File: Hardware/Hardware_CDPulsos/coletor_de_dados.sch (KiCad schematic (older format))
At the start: 1 part

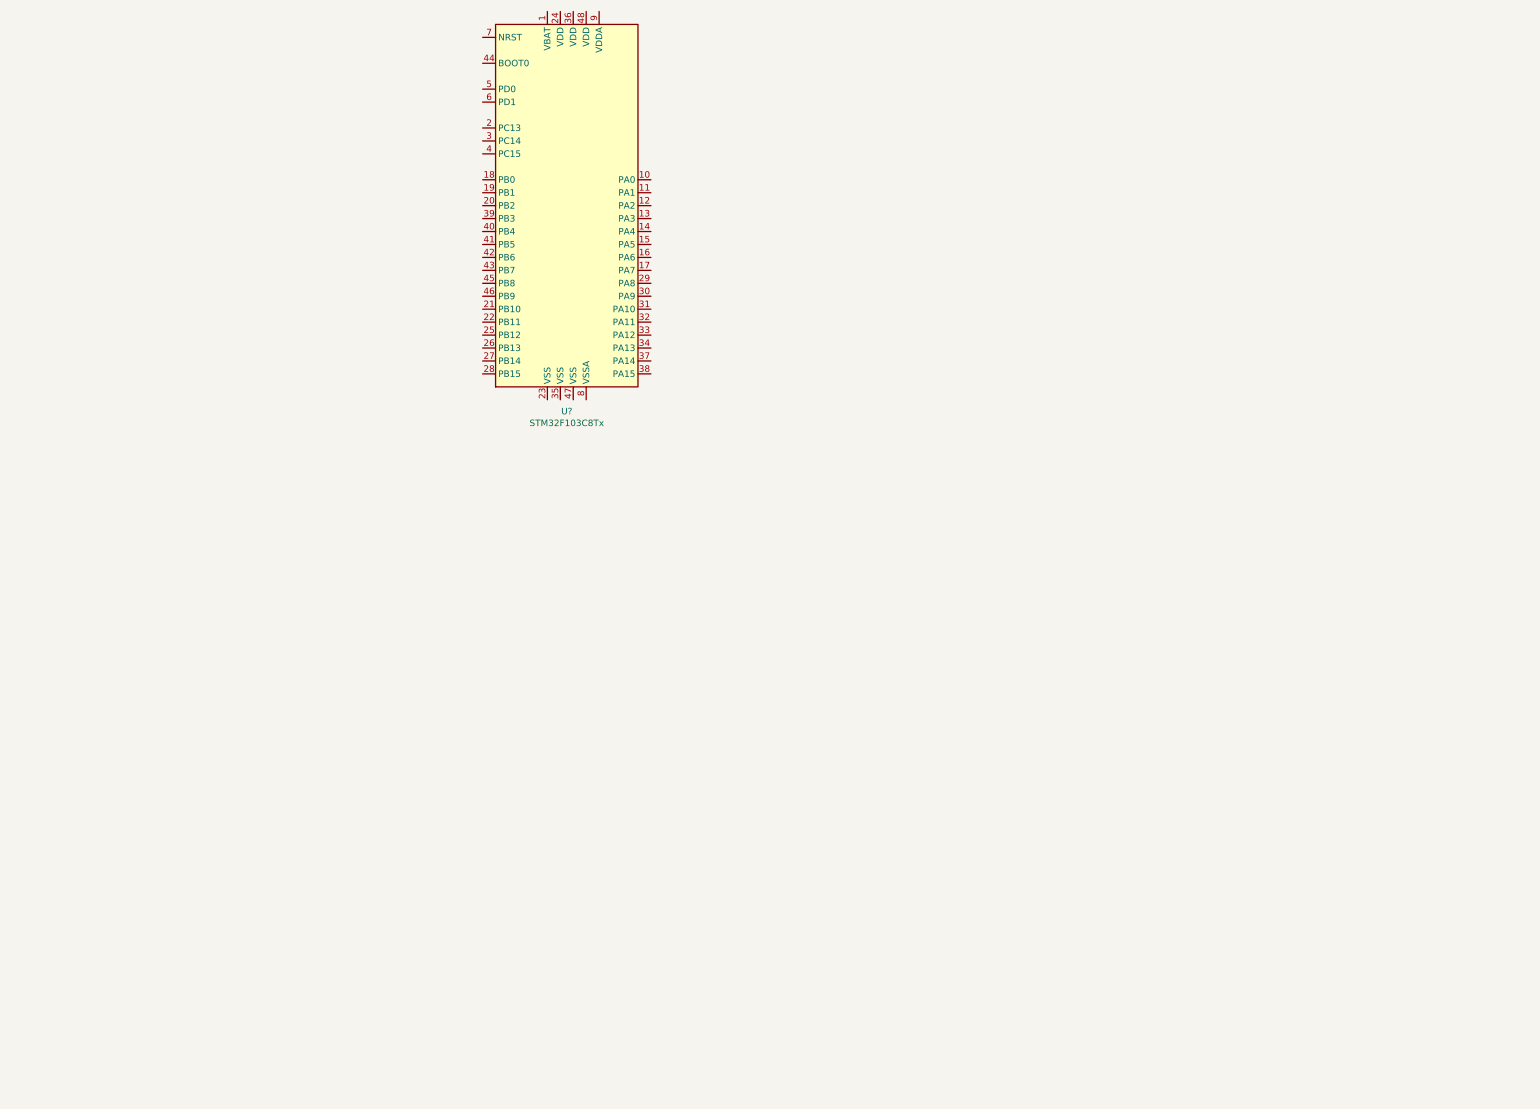
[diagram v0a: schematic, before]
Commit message: Esquecemos de adicionar a referencia de esquematico do sd card
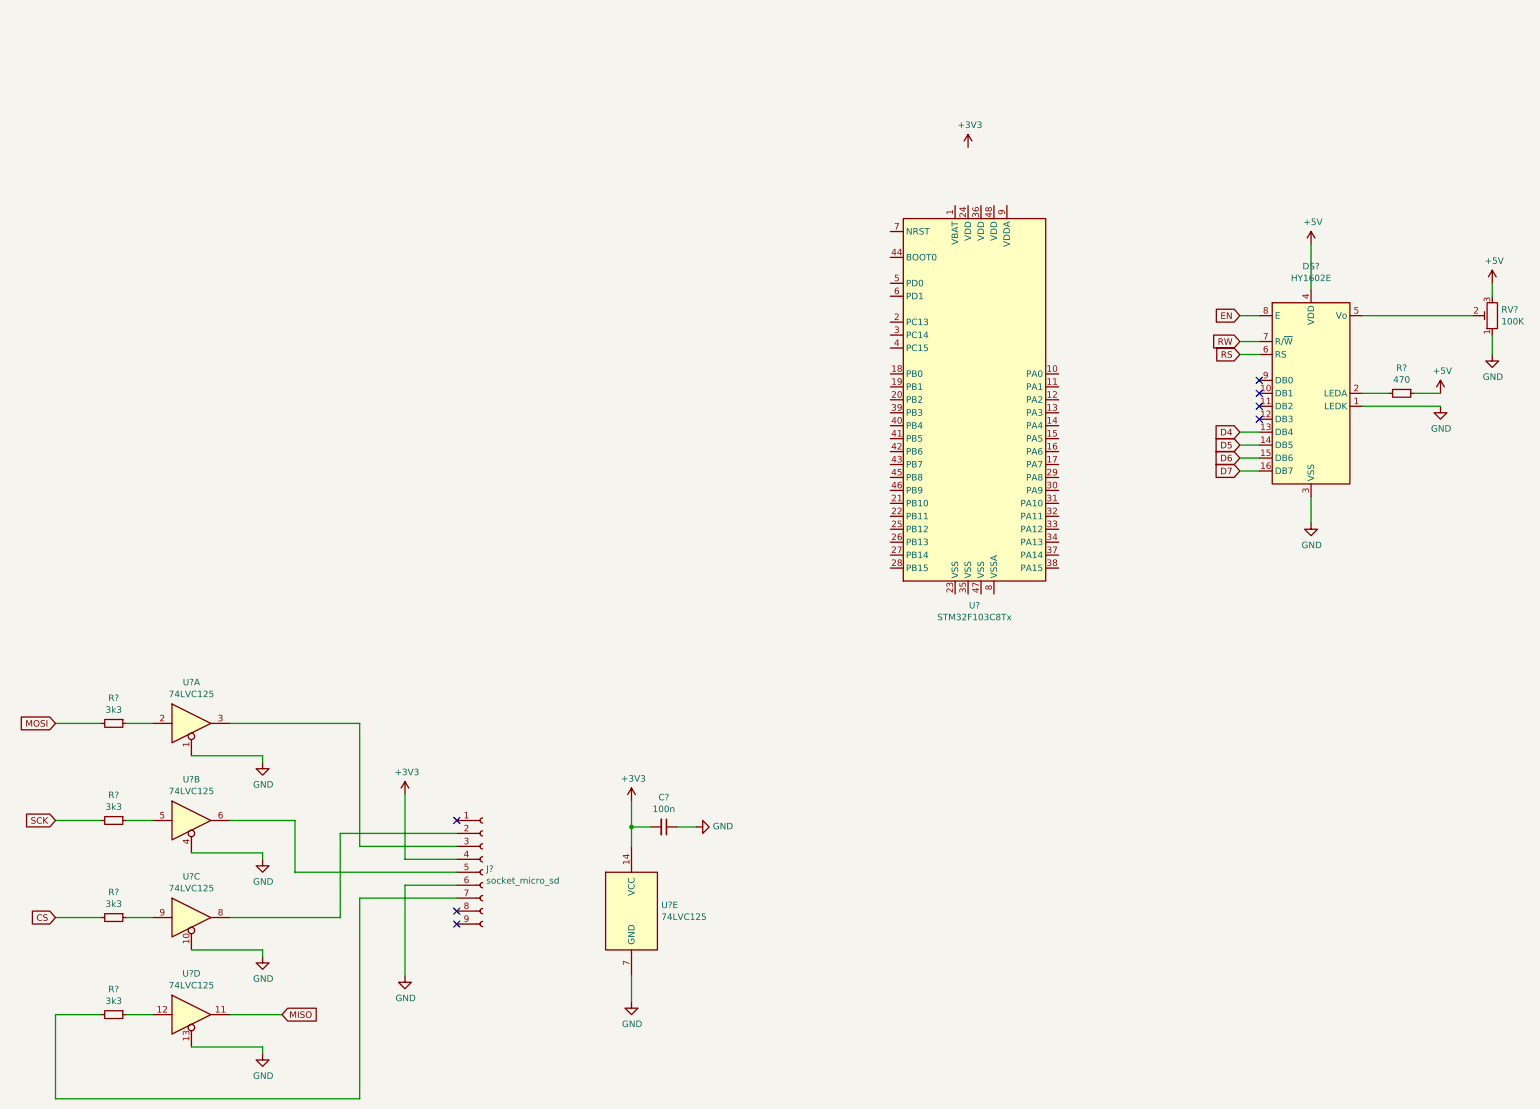
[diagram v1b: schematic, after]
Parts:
- added C?: 100n, symbol Device:C_Small
- added DS?: HY1602E, Display:HY1602E, symbol Display_Character:HY1602E
- added J?: socket_micro_sd, symbol Connector:Conn_01x09_Female
- added R?: 470, symbol Device:R_Small
- added R? (x4): 3k3, symbol Device:R_Small
- added RV?: 100K, symbol Device:R_POT_TRIM
- added U? (x5): 74LVC125, symbol 74xx:74LVC125
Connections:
- new net: DS?.2 (LEDA), R?.2
- new net: DS?.5 (Vo), RV?.2
- new net: R?.1, U?.2
- new net: J?.3 (Pin_3), U?.3
- new net: R?.1, U?.5
- new net: J?.5 (Pin_5), U?.6
- new net: J?.2 (Pin_2), U?.8
- new net: R?.1, U?.9
- new net: R?.1, U?.12
- new net: J?.7 (Pin_7), R?.2
- new net +3V3: C?.2, J?.4 (Pin_4), U?.14 (VCC)
- new net +5V: DS?.4 (VDD), R?.1, RV?.3
- new net CS: R?.2
- new net D4: DS?.13 (DB4)
- new net D5: DS?.14 (DB5)
- new net D6: DS?.15 (DB6)
- new net D7: DS?.16 (DB7)
- new net EN: DS?.8 (E)
- new net GND: C?.1, DS?.1 (LEDK), DS?.3 (VSS), J?.6 (Pin_6), RV?.1, U?.1, U?.10, U?.13, U?.4, U?.7 (GND)
- new net MISO: U?.11
- new net MOSI: R?.2
- new net RS: DS?.6 (RS)
- new net RW: DS?.7 (R/~W)
- new net SCK: R?.2
- no-connect marks 0 -> 7
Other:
- moved on the sheet: U?
